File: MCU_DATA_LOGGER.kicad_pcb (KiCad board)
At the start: 4 copper layers, 49.3 x 31.2 mm, 29 parts, among them J1 Conn_01x04_Male, J2 Conn_01x04_Male, J3 Conn_01x09_Male, J4 Conn_02x03_Odd_Even, U1 DS1337S+, U2 24LC1025, U3 24LC1025, U4 ATMEGA328P-AU, Y1 32.768 KHz, Y2 16 MHz

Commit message: 2layer recovery.
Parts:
- moved D3 31.8 mm to (107.7, 84.6)
- moved C1 29.6 mm to (113.3, 99.6)
- moved R6 29.6 mm to (113.3, 95.2)
- moved Y2 29.6 mm to (97.8, 103.9)
- moved BT1 29.6 mm to (78.5, 90.9)
- moved J3 29.6 mm to (81.7, 110.2)
- moved U2 29.6 mm to (85.8, 93.6)
- moved U3 29.6 mm to (85.9, 85.3)
- moved C2 29.6 mm to (113.3, 90.4)
- moved J4 29.6 mm to (117.6, 88.9)
- moved R7 29.6 mm to (107.7, 90.4)
- moved C3 29.6 mm to (96.8, 85.6)
- moved C4 29.6 mm to (93.0, 85.6)
- moved C5 29.6 mm to (100.6, 85.6)
- moved D2 29.6 mm to (113.0, 84.6)
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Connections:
- J1 pad 4: /SCL -> /SCK
- R3 pad 2: /SCL -> /SCK
- U1 pad 6: /SCL -> /SCK
- U2 pad 6: /SCL -> /SCK
- U3 pad 6: /SCL -> /SCK
- U4 pad 28: /SCL -> /SCK
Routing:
- net /Vcc: track 55.2 -> 203.0 mm, vias 9 -> 6
- net /SCK: track 28.5 -> 109.7 mm, vias 1 -> 8
- net /SCL: track 75.0 -> 0.00 mm, vias 3 -> 0
- net GND: track 40.8 -> 100.2 mm, vias 12 -> 9
- net Net-(C4-Pad2): track 17.1 -> 35.1 mm
- net /MISO: track 28.0 -> 43.5 mm, vias 2 -> 4
- net /SDA: track 57.4 -> 67.0 mm
- net Net-(D2-Pad1): track 3.82 -> 11.6 mm
- net /D8: track 19.3 -> 11.9 mm, vias 0 -> 1
- net Net-(C3-Pad2): track 23.1 -> 30.2 mm, vias 3 -> 2
- net /Tx: track 36.0 -> 30.7 mm, vias 0 -> 1
- net /D7: track 15.9 -> 12.6 mm, vias 0 -> 1
- net /D2: track 29.5 -> 32.1 mm
- net /RESET: track 22.9 -> 25.4 mm
- net Net-(R1-Pad2): track 7.48 -> 9.21 mm
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- removed copper zone on In2.Cu, net /Vcc
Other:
- board text removed: "0,2000 mm / 0,0000 mm"
- board text removed: "0,3000 mm"
- board text removed: "4"
- board text removed: "4,6900 mm"
- board text removed: "49,3760 mm x 31,3420 mm"
- board text removed: "BOARD CHARACTERISTICS"
- board text removed: "Board Thickness:"
- board text removed: "Board overall dimensions:"
- board text removed: "Castellated pads:"
- board text removed: "Copper Finish:"
- board text removed: "Copper Layer Count:"
- board text removed: "Edge card connectors:"
- board text removed: "Impedance Control:"
- board text removed: "Min hole diameter:"
- board text removed: "Min track/spacing:"
- board text removed: "No"
- board text removed: "None"
- board text removed: "Plated Board Edge:"

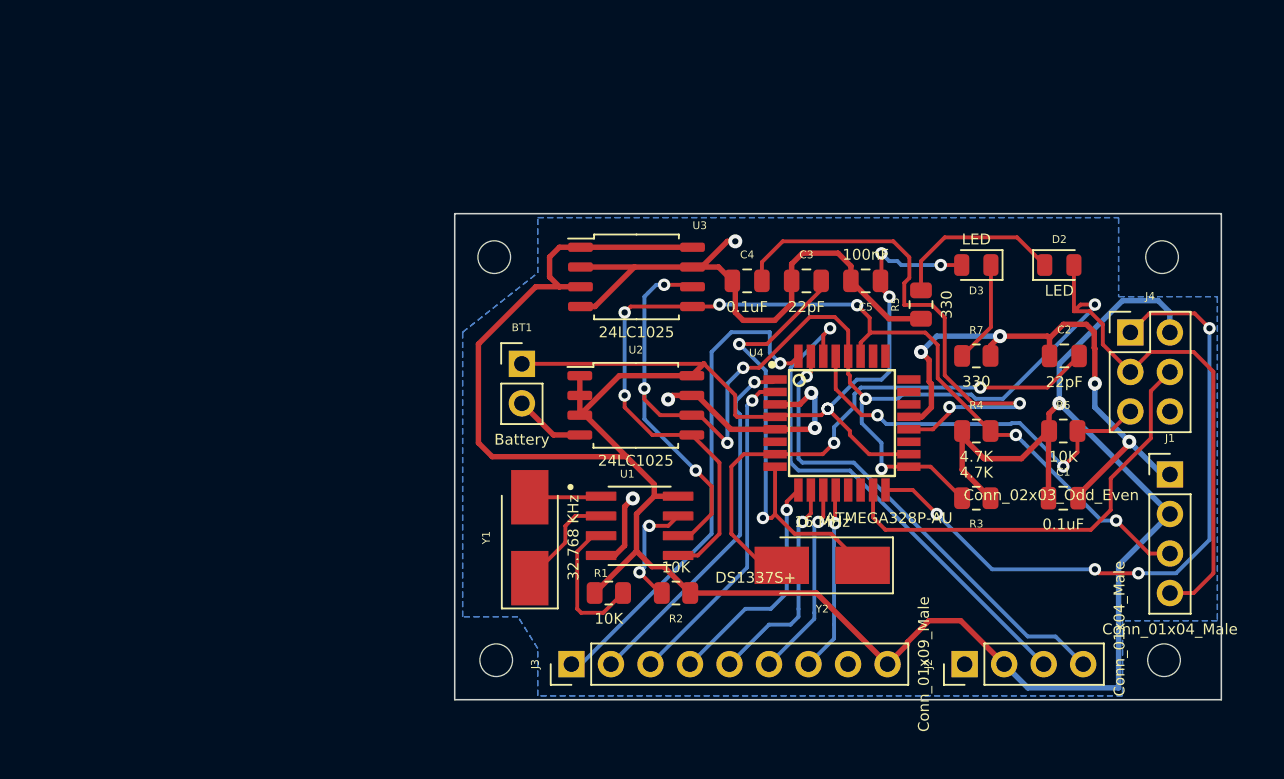
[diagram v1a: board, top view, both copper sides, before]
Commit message: 2layer SCL & SCK bug - fix.
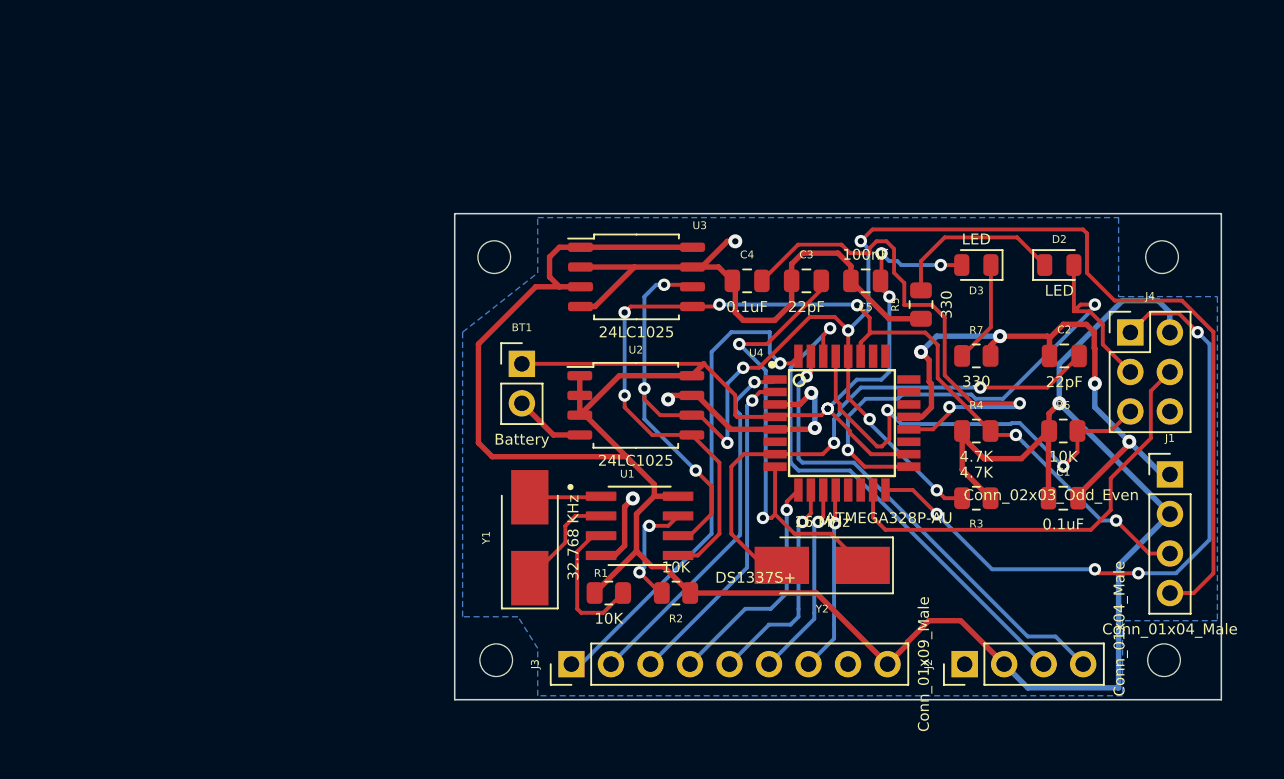
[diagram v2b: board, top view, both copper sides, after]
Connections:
- J1 pad 4: /SCK -> /SCL
- R3 pad 2: /SCK -> /SCL
- U1 pad 6: /SCK -> /SCL
- U2 pad 6: /SCK -> /SCL
- U3 pad 6: /SCK -> /SCL
- U4 pad 28: /SCK -> /SCL
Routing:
- net /SCL: track 0.00 -> 109.8 mm, vias 0 -> 9
- net /SCK: track 109.7 -> 36.2 mm, vias 8 -> 2
- net /RESET: track 25.4 -> 29.2 mm
- net Net-(C4-Pad2): track 35.1 -> 34.5 mm
- net /MISO: track 43.5 -> 42.9 mm
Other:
- copper layers 4 -> 2
- board text added: "0,2000 mm / 0,0000 mm"
- board text added: "0,3000 mm"
- board text added: "1,6000 mm"
- board text added: "2"
- board text added: "49,3760 mm x 31,3420 mm"
- board text added: "BOARD CHARACTERISTICS"
- board text added: "Board Thickness:"
- board text added: "Board overall dimensions:"
- board text added: "Castellated pads:"
- board text added: "Copper Finish:"
- board text added: "Copper Layer Count:"
- board text added: "Edge card connectors:"
- board text added: "Impedance Control:"
- board text added: "Min hole diameter:"
- board text added: "Min track/spacing:"
- board text added: "No"
- board text added: "None"
- board text added: "Plated Board Edge:"
